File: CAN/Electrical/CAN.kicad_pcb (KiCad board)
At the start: 4 copper layers, 26 x 30 mm, 32 parts, among them J1 Conn_01x05, P1 USB_C_Plug_USB2.0, SW1 Reset, U1 ESP32-C3-MINI-1, U2 AP2112K-3.3, U3 SN65HVD230, U4 FODM217D

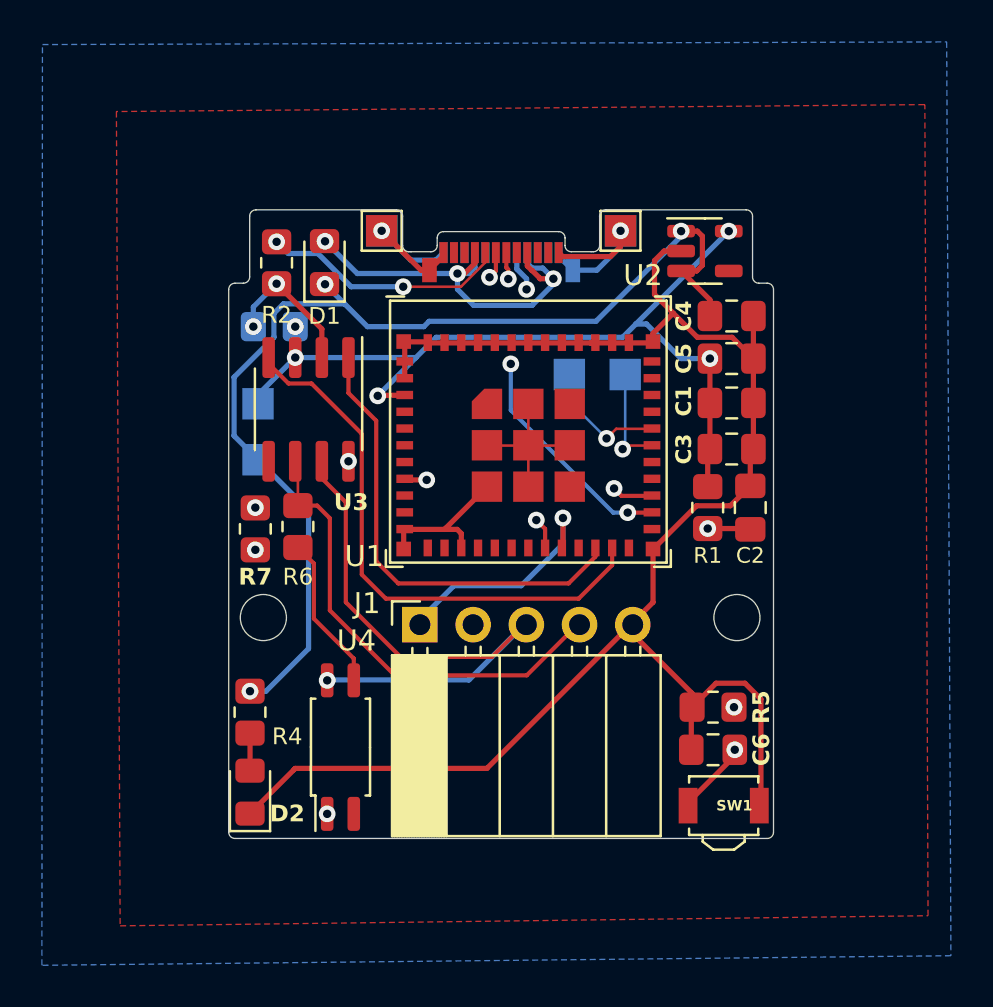
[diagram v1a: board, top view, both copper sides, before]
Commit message: Replaced ESP32 Moduole with ESP32-C3
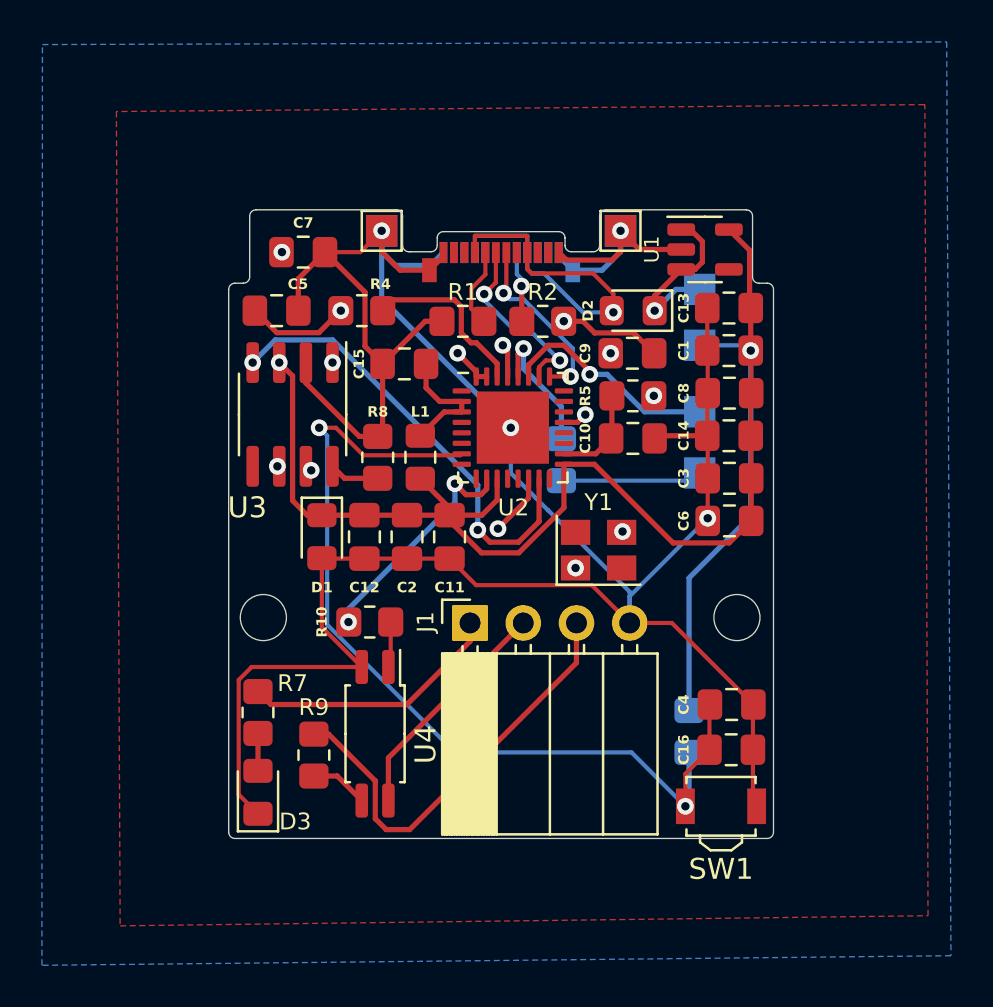
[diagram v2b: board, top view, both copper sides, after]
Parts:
- added C10: 1uF, Capacitor_SMD:C_0805_2012Metric_Pad1.18x1.45mm_HandSolder, F.Cu at (81.5, 97.3)
- added C11: 0.1uF, Capacitor_SMD:C_0805_2012Metric_Pad1.18x1.45mm_HandSolder, F.Cu at (72.8, 102.0)
- added C12: 0.1uF, Capacitor_SMD:C_0805_2012Metric_Pad1.18x1.45mm_HandSolder, F.Cu at (68.7, 102.0)
- added C13: 10uF, Capacitor_SMD:C_0805_2012Metric_Pad1.18x1.45mm_HandSolder, F.Cu at (86.1, 91.1)
- added C14: 0.1uF, Capacitor_SMD:C_0805_2012Metric_Pad1.18x1.45mm_HandSolder, F.Cu at (86.1, 97.2)
- added C15: 0.1uF, Capacitor_SMD:C_0805_2012Metric_Pad1.18x1.45mm_HandSolder, F.Cu at (70.6, 93.7)
- added C16: 0.1uF, Capacitor_SMD:C_0805_2012Metric_Pad1.18x1.45mm_HandSolder, F.Cu at (86.2, 112.1)
- added C7: 10uF, Capacitor_SMD:C_0805_2012Metric_Pad1.18x1.45mm_HandSolder, F.Cu at (65.8, 88.4)
- added C8: 10uF, Capacitor_SMD:C_0805_2012Metric_Pad1.18x1.45mm_HandSolder, F.Cu at (86.1, 95.1)
- added C9: TBD, Capacitor_SMD:C_0805_2012Metric_Pad1.18x1.45mm_HandSolder, F.Cu at (81.5, 93.2)
- added D3: LED, LED_SMD:LED_0805_2012Metric_Pad1.15x1.40mm_HandSolder, F.Cu at (63.6, 114.2)
- added L1: 2nH, Inductor_SMD:L_0805_2012Metric_Pad1.15x1.40mm_HandSolder, F.Cu at (71.4, 98.2)
- added R10: 20R, Resistor_SMD:R_0805_2012Metric_Pad1.20x1.40mm_HandSolder, F.Cu at (69.0, 106.0)
- added R8: 10k, Resistor_SMD:R_0805_2012Metric_Pad1.20x1.40mm_HandSolder, F.Cu at (69.3, 98.2)
- added R9: 120R, Resistor_SMD:R_0805_2012Metric_Pad1.20x1.40mm_HandSolder, F.Cu at (66.3, 112.4)
- added Y1: 40MHz, Crystal:Crystal_SMD_TXC_7M-4Pin_3.2x2.5mm, F.Cu at (79.9, 102.6)
- C2: value 1uF -> 0.1uF
- C3: value 0.1uF -> 1uF
- C4: value 10uF -> 1uF
- C5: value 10uF -> TBD
- C6: value 0.1uF -> 10nF
- D1: value D_Schottky -> ESD
- D2: value LED -> D_Schottky; footprint LED_SMD:LED_0805_2012Metric_Pad1.15x1.40mm_HandSolder -> Diode_SMD:D_0805_2012Metric_Pad1.15x1.40mm_HandSolder
- J1: value Conn_01x05 -> Conn_01x04; footprint Connector_PinSocket_2.54mm:PinSocket_1x05_P2.54mm_Horizontal -> Connector_PinSocket_2.54mm:PinSocket_1x04_P2.54mm_Horizontal
- R1: value 10k -> 5.1k
- R3: value 5.1k -> 10k
- R4: value 5.1k -> 0R
- R6: value 120R -> 499R; moved to B.Cu
- R7: value 20R -> 5.1k
- U1: value ESP32-C3-MINI-1 -> AP2112K-3.3; footprint Espressif:ESP32-C3-MINI-1U -> Package_TO_SOT_SMD:SOT-23-5
- U2: value AP2112K-3.3 -> ESP32-C3; footprint Package_TO_SOT_SMD:SOT-23-5 -> Package_DFN_QFN:QFN-32-1EP_5x5mm_P0.5mm_EP3.45x3.45mm
- moved D2 29.4 mm to (81.5, 91.2), turned to 180 degrees
- moved R3 27.7 mm to (84.2, 111.3), turned to -90 degrees
- moved TP5 22.6 mm to (84.7, 90.2)
- moved C5 21.8 mm to (64.5, 91.2)
- moved TP6 21.3 mm to (84.7, 92.8)
- moved R4 19.9 mm to (68.6, 91.2), turned to 0 degrees
- moved C4 18.5 mm to (86.2, 110.0)
- moved C2 16.4 mm to (70.7, 102.0), turned to -90 degrees
- moved R5 15.3 mm to (81.5, 95.2)
- moved R1 14.7 mm to (73.4, 91.7), turned to 180 degrees
- moved D1 13.1 mm to (66.7, 102.0), turned to -90 degrees
- moved R2 13.0 mm to (77.2, 91.7), turned to 0 degrees
- moved R6 13.0 mm to (78.1, 98.3)
- moved U2 12.5 mm to (75.8, 96.8)
- moved U1 12.1 mm to (85.0, 88.3)
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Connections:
- C2 pad 1: /EN -> +3.3V
- C3 pad 1: GND -> +3.3V
- C3 pad 2: +3.3V -> GND
- C4 pad 1: VBUS -> /EN
- C5 pad 1: +3.3V -> Net-(C5-Pad1)
- C6 pad 1: GND -> +3.3V
- C6 pad 2: /EN -> GND
- D1 pad 1: VBUS -> +3.3V
- D1 pad 2: Net-(D1-A) -> GND
- D2 pad 1: GND -> VBUS
- J1 pad 1: /GPIO6 -> VBUS
- J1 pad 2: VBUS -> CAN_H
- J1 pad 3: CAN_H -> CAN_L
- J1 pad 4: CAN_L -> GND
- P1 pad A4: Net-(D1-A) -> Net-(D2-A)
- P1 pad A9: Net-(D1-A) -> Net-(D2-A)
- P1 pad B4: Net-(D1-A) -> Net-(D2-A)
- P1 pad B9: Net-(D1-A) -> Net-(D2-A)
- R1 pad 1: +3.3V -> Net-(P1-CC)
- R1 pad 2: /EN -> GND
- R2 pad 1: Net-(P1-CC) -> Net-(P1-VCONN)
- R3 pad 1: Net-(P1-VCONN) -> +3.3V
- R3 pad 2: GND -> /EN
- R4 pad 1: VBUS -> Net-(C5-Pad1)
- R4 pad 2: Net-(D2-A) -> Net-(U2-XTAL_P)
- R5 pad 1: GND -> /VDD_SPI
- R5 pad 2: Net-(U3-Rs) -> Net-(U2-SPICS0/GPIO14)
- R6 pad 1: CAN_L -> Net-(U2-U0TXD/GPIO21)
- R6 pad 2: Net-(R6-Pad2) -> /TXD
- R7 pad 1: /TERM -> VBUS
- R7 pad 2: Net-(R7-Pad2) -> Net-(D3-A)
- U1 pad 1: GND -> VBUS
- U1 pad 3: +3.3V -> VBUS
- U1 pad 5: unconnected-(U1-GPIO2/ADC1_CH2-Pad5) -> +3.3V
- U2 pad 1: VBUS -> unconnected-(U2-LNA_IN-Pad1)
- U2 pad 2: GND -> Net-(C15-Pad2)
- U2 pad 3: VBUS -> Net-(C15-Pad2)
- U2 pad 5: +3.3V -> unconnected-(U2-XTAL_32K_N/ADC1_CH1-Pad5)
- U4 pad 1: Net-(R7-Pad2) -> Net-(R10-Pad2)
- U4 pad 3: Net-(R6-Pad2) -> Net-(R9-Pad2)
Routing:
- net +3.3V: track 40.5 -> 87.1 mm, vias 4 -> 3
- net GND: track 120.2 -> 154.5 mm, vias 4 -> 5
- net Net-(C5-Pad1): track 0.00 -> 24.3 mm, vias 0 -> 2
- net Net-(U3-Rs): track 24.7 -> 2.40 mm, vias 2 -> 0
- net Net-(D1-A): track 20.7 -> 0.00 mm, vias 3 -> 0
- net Net-(D2-A): track 1.79 -> 20.2 mm, vias 0 -> 1
- net Net-(U2-XTAL_N): track 0.00 -> 17.3 mm, vias 0 -> 3
- net CAN_L: track 22.2 -> 38.5 mm, vias 0 -> 1
- net Net-(R7-Pad2): track 16.0 -> 0.00 mm, vias 2 -> 0
- net /EN: track 33.0 -> 45.6 mm, vias 3 -> 2
- net /GPIO6: track 11.4 -> 0.00 mm, vias 1 -> 0
- net Net-(P1-VCONN): track 13.7 -> 3.38 mm, vias 2 -> 1
- net Net-(U2-XTAL_P): track 0.00 -> 8.29 mm
- net Net-(P1-CC): track 11.8 -> 3.81 mm, vias 2 -> 0
- net /D-: track 16.4 -> 8.78 mm, vias 3 -> 2
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
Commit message: Updated Schematic
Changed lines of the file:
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@@
         (effects (font (size 1 1) (thickness 0.15)))
+    )
+    (fp_text user "CAN_H" (at 0 0 90 unlocked) (layer "F.SilkS")
+        (effects (font (size 0.5 0.5) (thickness 0.1)))
+    )
+    (fp_text user "GND" (at 1.442 7.533 unlocked) (layer "F.SilkS")
+        (effects (font (size 0.5 0.5) (thickness 0.1)))
+    )
+    (fp_text user "5V" (at 1.696 0.421 unlocked) (layer "F.SilkS")
+        (effects (font (size 0.5 0.5) (thickness 0.1)))
+    )
+    (fp_text user "CAN_L" (at 1.442 4.993 unlocked) (layer "F.SilkS")
+        (effects (font (size 0.5 0.5) (thickness 0.1)))
     )
     (fp_text user "${REFERENCE}" (at -5.775 3.81) (layer "F.Fab")
